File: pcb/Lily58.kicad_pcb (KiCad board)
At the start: 2 copper layers, 142.5 x 106.3 mm, 123 parts, among them J1 LED, J2 4PIN, P1 i2c_pin, P2 i2c_pin, P3 ICSP, P4 OLED, SW1 SW_PUSH, SW10 SW_PUSH, SW11 SW_PUSH, SW12 SW_PUSH, SW13 SW_PUSH, SW14 SW_PUSH, SW15 SW_PUSH, SW16 SW_PUSH, SW17 SW_PUSH, SW18 SW_PUSH, SW19 SW_PUSH, SW2 SW_PUSH, SW20 SW_PUSH, SW21 SW_PUSH, SW22 SW_PUSH, SW23 SW_PUSH, SW24 SW_PUSH, SW25 SW_PUSH, SW26 SW_PUSH, SW27 SW_PUSH, SW28 SW_PUSH, SW29 SW_PUSH, SW3 SW_PUSH, SW4 SW_PUSH, SW5 SW_PUSH, SW6 SW_PUSH, SW7 SW_PUSH, SW8 SW_PUSH, SW9 SW_PUSH, U1 ProMicro

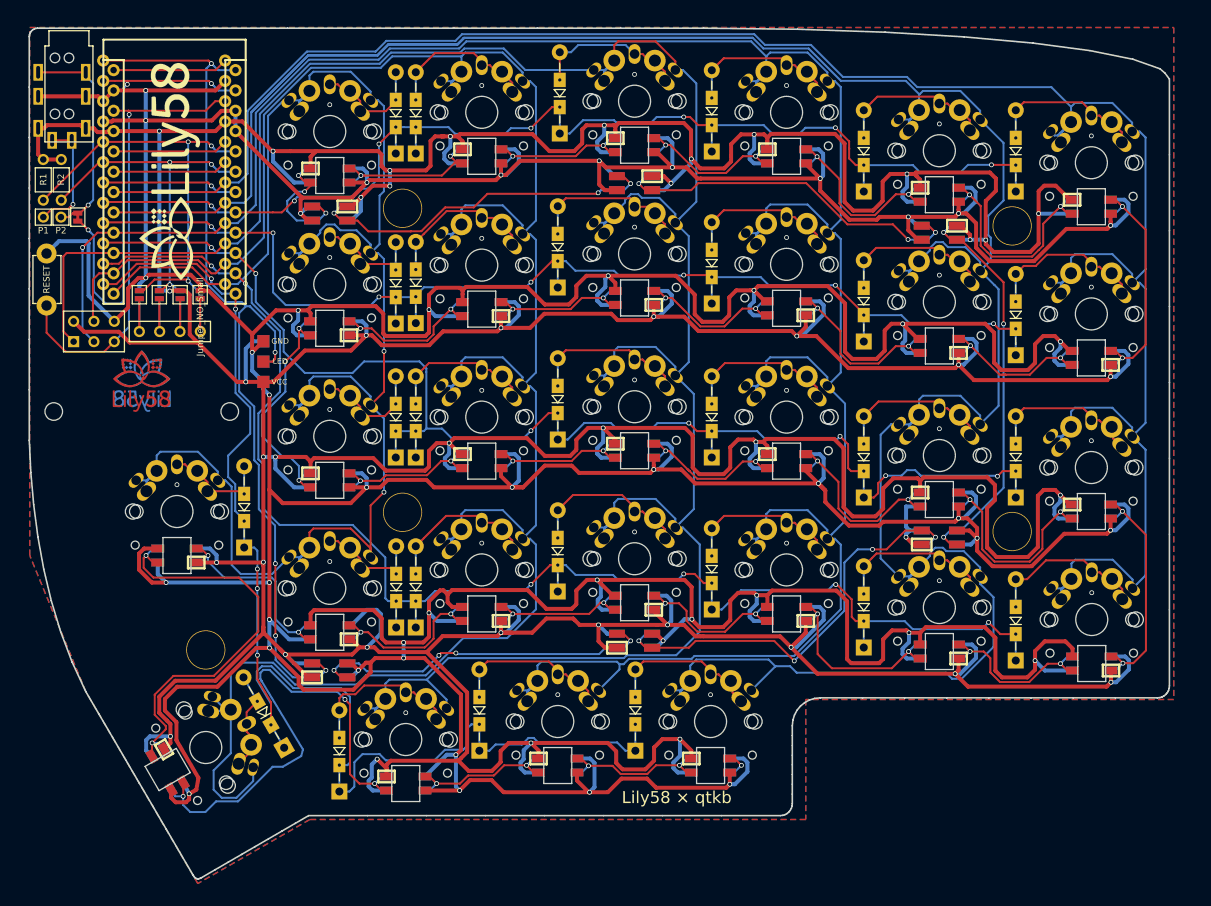
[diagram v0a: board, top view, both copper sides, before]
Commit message: Added Encoder and 1 led
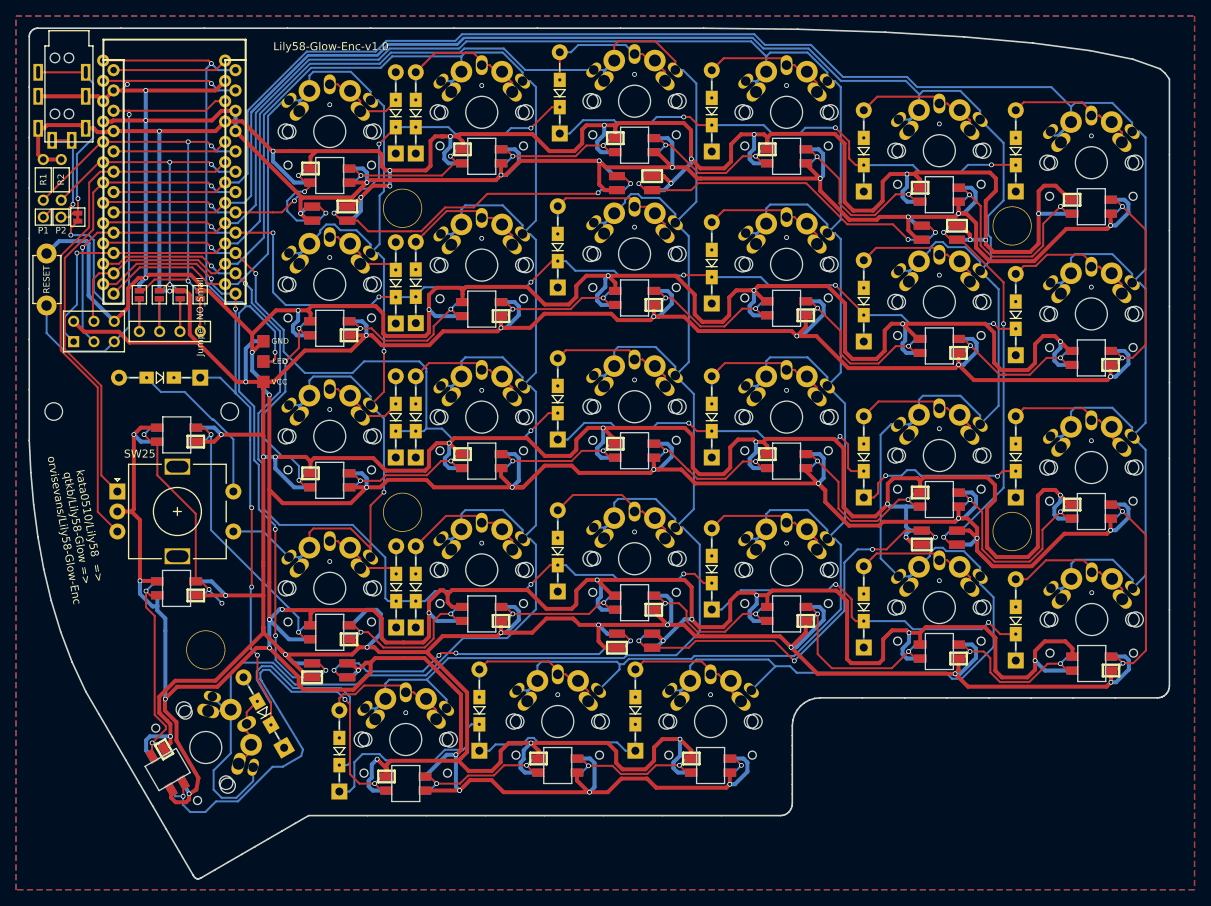
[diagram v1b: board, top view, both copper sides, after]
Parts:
- removed G*** (x2): LOGO, Lily58-footprint:lily58_logo_2
- removed G*** (x2): LOGO, Lily58-footprint:lily58_logo_3
- added L26: SK6812mini, Lily58-footprint:SK6812MINI_rev, F.Cu at (101.3, 107.1)
- SW25: value SW_PUSH -> Rotary_Encoder_Switch; footprint Lily58-footprint:MX_PG1350_FLIP_HOLES_18mm -> Lily58-footprint:RotaryEncoder_Alps_EC11E-Switch_Vertical_H20mm
- moved D25 19.3 mm to (99.3, 80.8), turned to 180 degrees
- moved L25 15.1 mm to (101.3, 87.9)
- moved SW25 7.86 mm to (94.0, 95.0)
- renumbered L26 to L27, L27 to L28, L28 to L29, L29 to L30, L30 to L31, L31 to L32, L32 to L33, L33 to L34, L34 to L35, L35 to L36
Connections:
- L27 pad 3: Net-(L25-Pad1) -> Net-(L26-Pad1)
- U1 pad 19: Net-(U1-Pad19) -> enc2
- U1 pad 7: Net-(U1-Pad7) -> enc1
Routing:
- net enc2: track 0.00 -> 66.1 mm
- net enc1: track 0.00 -> 60.4 mm, vias 0 -> 1
- net col5: track 215.5 -> 185.4 mm
- net Net-(L26-Pad1): track 0.00 -> 27.8 mm, vias 0 -> 2
- net GND: track 1068.1 -> 1095.1 mm, vias 74 -> 73
- net Net-(L25-Pad1): track 52.5 -> 30.0 mm, vias 2 -> 3
- net Net-(U1-Pad7): track 17.0 -> 0.00 mm, vias 1 -> 0
- net VCC: track 1030.4 -> 1045.9 mm, vias 43 -> 44
- net Net-(U1-Pad19): track 14.4 -> 0.00 mm
- net Net-(L19-Pad1): track 25.9 -> 37.5 mm
- net Net-(D25-Pad2): track 14.1 -> 24.0 mm
- net row4: track 167.1 -> 176.0 mm
- net DATA: track 59.0 -> 60.9 mm
- net col3: track 300.9 -> 300.2 mm, vias 0 -> 1
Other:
- outline, holes or cut-outs redrawn
- board text added: "Lily58-Glow-Enc-v1.0"
- board text added: "kata0510/Lily58 => qtkb/Lily58-Glow => orvisevans/Lily58-Glow-Enc"
- board text removed: "Glow"
- board text removed: "Lily58 × qtkb"
